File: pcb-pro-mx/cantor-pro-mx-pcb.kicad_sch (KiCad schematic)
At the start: 43 parts, among them J1 TRRS, K00 KEYSW, K01 KEYSW, K02 KEYSW, K03 KEYSW, K04 KEYSW, K05 KEYSW, K10 KEYSW, K11 KEYSW, K12 KEYSW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

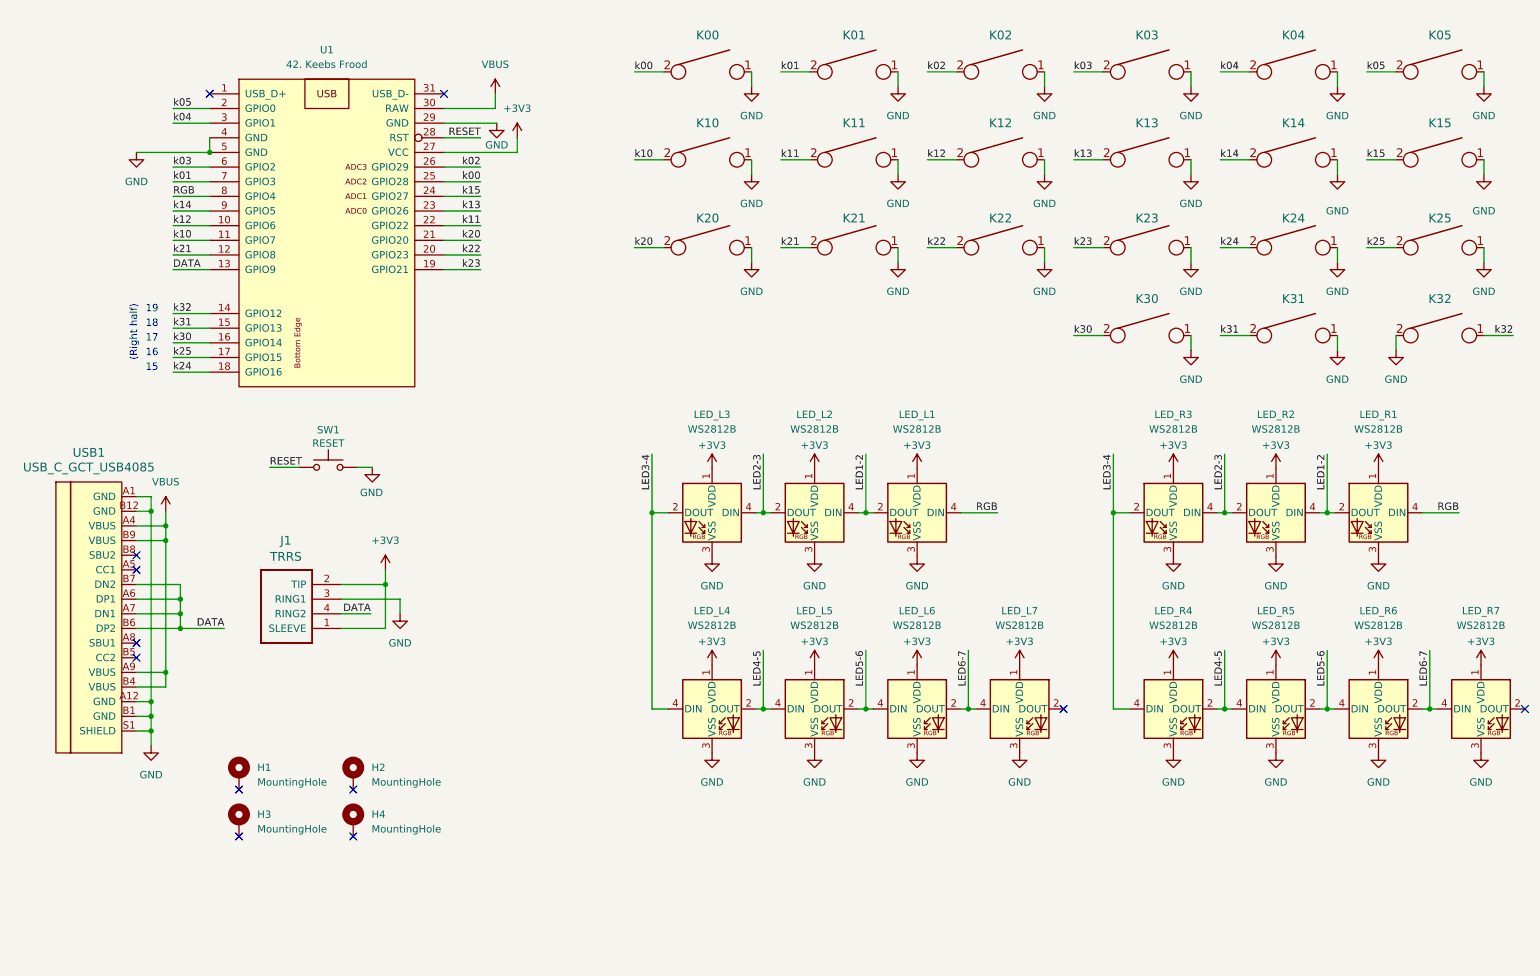
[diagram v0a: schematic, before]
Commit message: Update Cantor Pro Frood to v3.1
* Support for Frood and nice!nano
* Add battery contacts and power switch
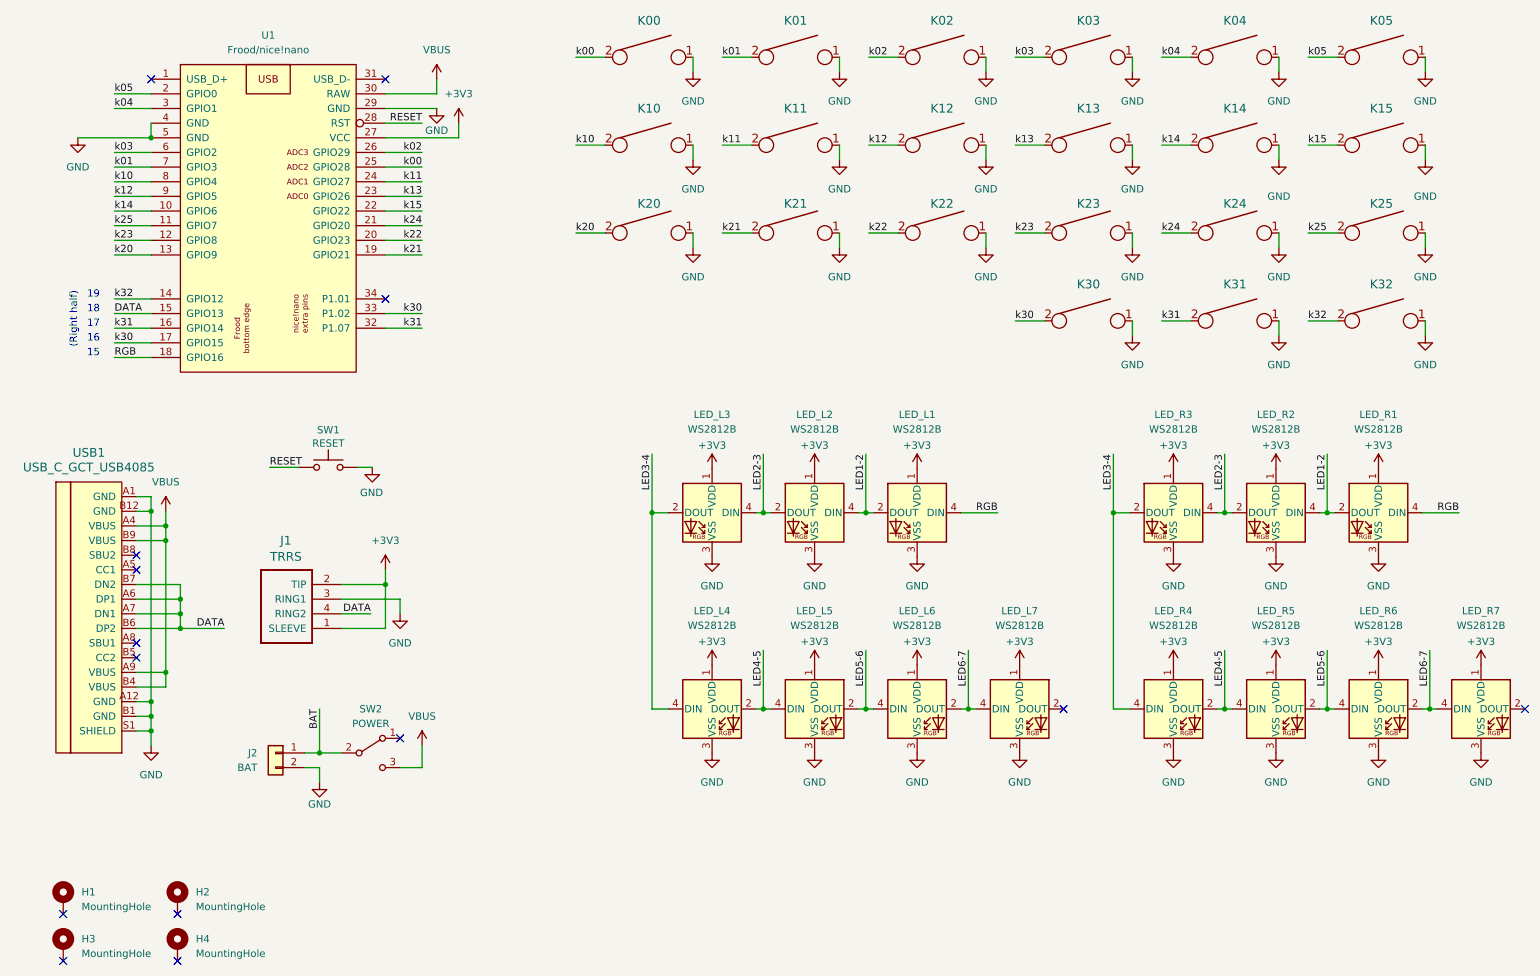
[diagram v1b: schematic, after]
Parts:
- removed U1: 42. Keebs Frood, 42keebs:Frood_PinHeader_2x12+5_P2.54mm_Dual_VAligned, symbol 42keebs:Frood
- added J2: BAT, 42keebs:ProMicro_Battery_Connector_Double_Sided_wide, symbol Connector_Generic:Conn_01x02
- added SW2: POWER, 42keebs:SW_SPDT_PCM12_double_sided_shifted_with_edge_cutouts, symbol Switch:SW_SPDT
- added U1: Frood/nice!nano, 42keebs:Frood_nice-nano_PinHeader_2x12+5+3_P2.54mm_Dual_V-aligned, symbol 42keebs:Frood+nice!nano
- LED_L1, LED_L2, LED_L3, LED_L4, LED_L5, LED_L6, LED_L7, LED_R1, LED_R2, LED_R3, LED_R4, LED_R5, LED_R6, LED_R7: footprint LED_SMD:LED_WS2812B_PLCC4_5.0x5.0mm_P3.2mm -> 42keebs:LED_WS2812B_PLCC4_5.0x5.0mm_P3.2mm_w_cutout
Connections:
- net +3V3: now also U1.27 (VCC)
- net DATA: now also U1.15 (GPIO13)
- net GND: now also K32.1, J2.2 (Pin_2), U1.29 (GND), U1.4 (GND), U1.5 (GND); no longer K32.2
- net RESET: now also U1.28 (RST)
- net RGB: now also U1.18 (GPIO16)
- net VBUS: now also SW2.3 (C), U1.30 (RAW)
- net k00: now also U1.25 (GPIO28)
- net k01: now also U1.7 (GPIO3)
- net k02: now also U1.26 (GPIO29)
- net k03: now also U1.6 (GPIO2)
- net k04: now also U1.3 (GPIO1)
- net k05: now also U1.2 (GPIO0)
- net k10: now also U1.8 (GPIO4)
- net k11: now also U1.24 (GPIO27)
- net k12: now also U1.9 (GPIO5)
- net k13: now also U1.23 (GPIO26)
- net k14: now also U1.10 (GPIO6)
- net k15: now also U1.22 (GPIO22)
- net k20: now also U1.13 (GPIO9)
- net k21: now also U1.19 (GPIO21)
- net k22: now also U1.20 (GPIO23)
- net k23: now also U1.12 (GPIO8)
- net k24: now also U1.21 (GPIO20)
- net k25: now also U1.11 (GPIO7)
- net k30: now also U1.17 (GPIO15), U1.33 (P1.02)
- net k31: now also U1.16 (GPIO14), U1.32 (P1.07)
- net k32: now also K32.2, U1.14 (GPIO12); no longer K32.1
- new net BAT: J2.1 (Pin_1), SW2.2 (B)
- no-connect marks 12 -> 14
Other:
- moved on the sheet: H1, H2, H3, H4

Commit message: Remove LEDs
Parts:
- removed LED_L1, LED_L2, LED_L3, LED_L4, LED_L5, LED_L6, LED_L7, LED_R1, LED_R2, LED_R3, LED_R4, LED_R5, LED_R6, LED_R7: WS2812B, 42keebs:LED_WS2812B_PLCC4_5.0x5.0mm_P3.2mm_w_cutout, symbol LED:WS2812B
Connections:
- net RGB: no longer names the net of U1.18 (GPIO16)
- no-connect marks 14 -> 13
